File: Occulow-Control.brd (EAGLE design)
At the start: 38.1 x 104.1 mm, 44 parts, among them T1 DMP3010LK3, T2 DMP3010LK3, T3 DMP3010LK3

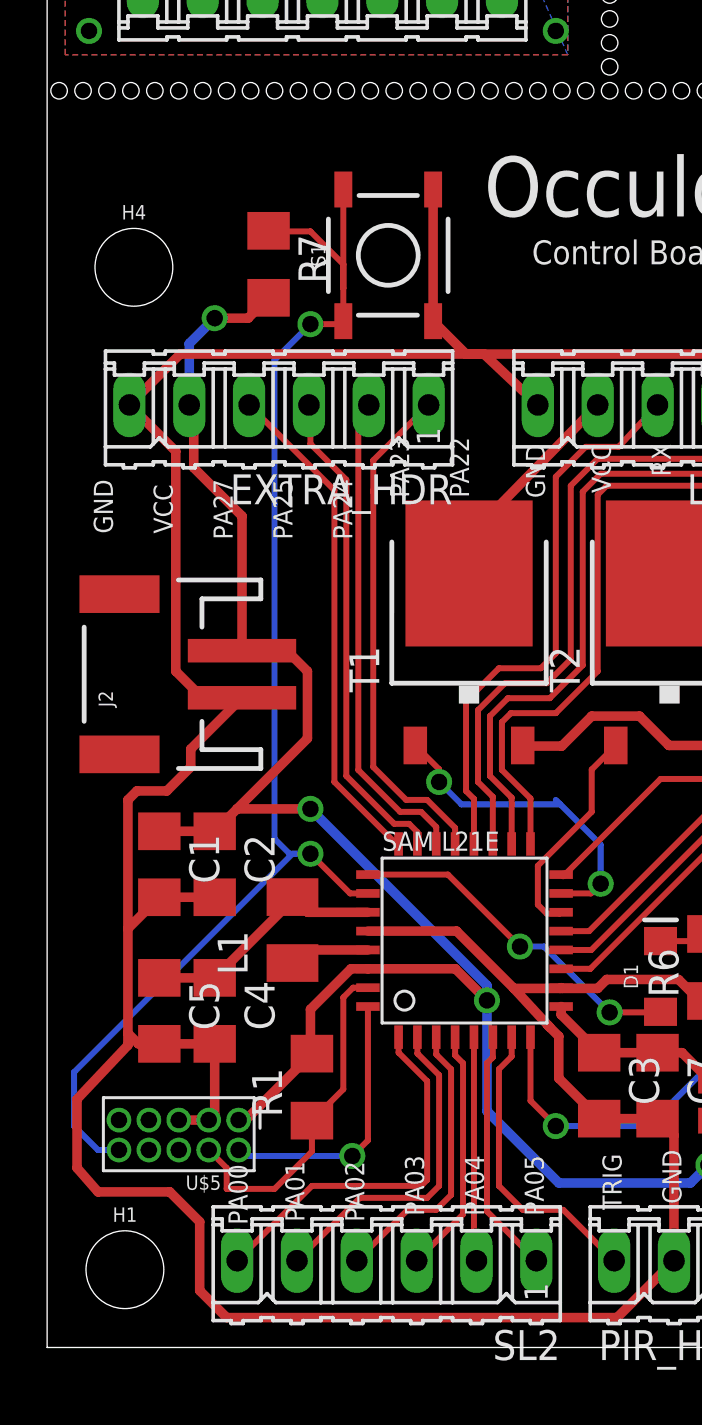
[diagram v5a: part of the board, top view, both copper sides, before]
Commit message: Replaced extra header with JTAG and i2c headers. Fixes #4
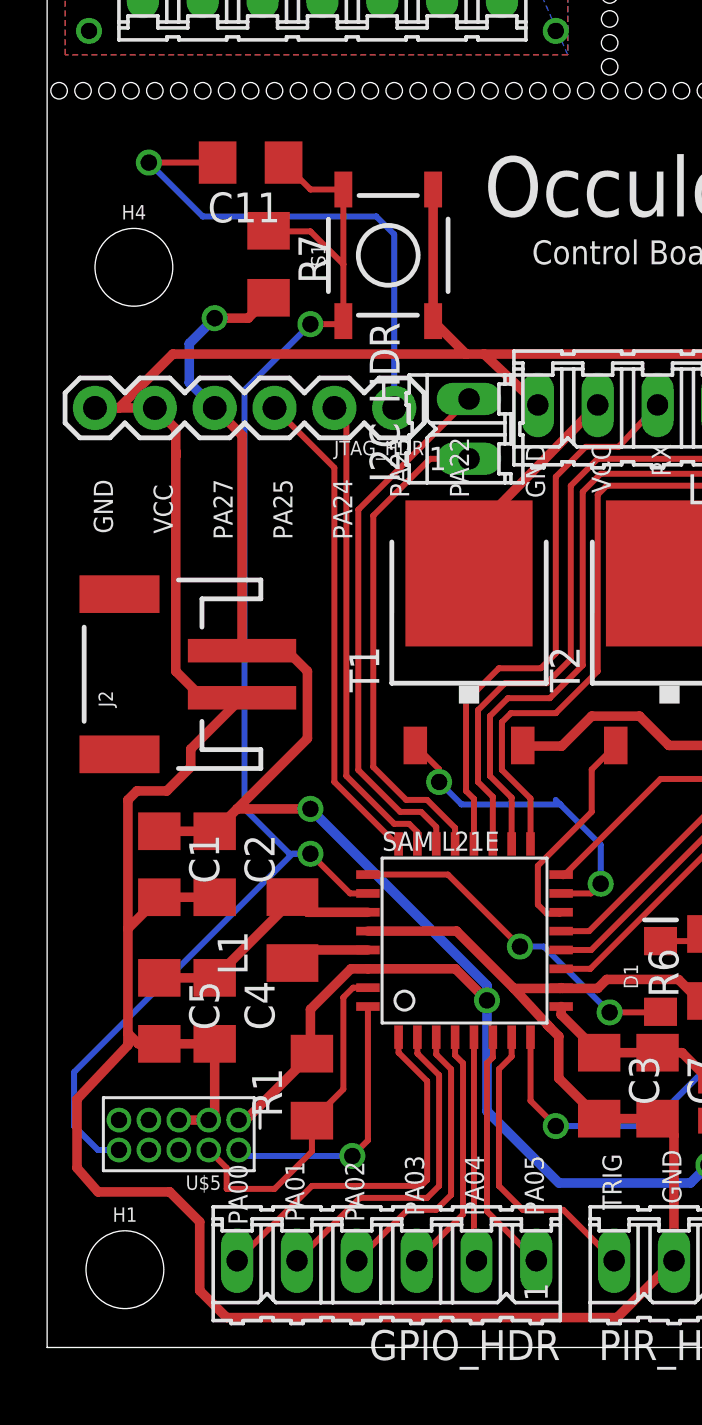
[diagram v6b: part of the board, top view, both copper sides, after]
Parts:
- removed EXTRA_HDR: (no value), con-amp-quick:06P
- added C11: 100nF, rcl:C1206
- added I2C_HDR: (no value), con-amp-quick:02P
- added JTAG_HDR: (no value), SparkFun-Connectors:1X06
- renumbered SL2 to GPIO_HDR
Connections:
- new net DTR: C11.2, JTAG_HDR.1
- net !RESET: now also C11.1
- net GND: now also JTAG_HDR.5, JTAG_HDR.6; no longer EXTRA_HDR.6
- net PA22: now also I2C_HDR.1; no longer EXTRA_HDR.1
- net PA23: now also I2C_HDR.2; no longer EXTRA_HDR.2
- net PA24: now also JTAG_HDR.2; no longer EXTRA_HDR.3
- net PA25: now also JTAG_HDR.3; no longer EXTRA_HDR.4
- net VCC: now also JTAG_HDR.4; no longer EXTRA_HDR.5
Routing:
- net DTR: track 0.00 -> 22.0 mm, vias 0 -> 1
- net !RESET: track 57.7 -> 60.7 mm
- net PA23: track 20.7 -> 22.7 mm
- net GND: track 168.6 -> 170.5 mm
- net PA25: track 21.6 -> 20.7 mm
- net PA22: track 21.6 -> 21.0 mm
- net PA24: track 20.9 -> 20.3 mm

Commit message: Created 2 wire trap lib, placed in schematic
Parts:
- removed J2: (no value), SparkFun-Connectors:JST-2-SMD
- added U$7: MINI-LITE-TRAP, lite-trap:MINI-LITE-TRAP
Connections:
- net GND: now also U$7.3, U$7.4; no longer J2.1
- net VCC: now also U$7.1, U$7.2; no longer J2.2
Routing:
- net GND: track 170.5 -> 149.6 mm
- net VCC: track 107.9 -> 88.5 mm
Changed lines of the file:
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@@
 <?xml version="1.0" encoding="utf-8"?>
 <!DOCTYPE eagle SYSTEM "eagle.dtd">
-<eagle version="8.0.2">
+<eagle version="8.1.0">
 <drawing>
 <settings>
@@
 <setting verticaltext="up"/>
 </settings>
-<grid distance="0.01" unitdist="inch" unit="inch" style="lines" multiple="1" display="no" altdistance="0.005" altunitdist="inch" altunit="inch"/>
+<grid distance="1" unitdist="mm" unit="mm" style="lines" multiple="1" display="no" altdistance="0.05" altunitdist="mm" altunit="mm"/>
 <layers>
 <layer number="1" name="Top" color="4" fill="1" visible="yes" active="yes"/>
@@
 <attribute name="OC_NEWARK" value="unknown" x="34.7345" y="26.4795" size="1.778" layer="27" rot="R90" display="off"/>
 </element>
-<element name="J2" library="SparkFun-Connectors" package="JST-2-SMD" value="" x="4.572" y="28.575" rot="R90">
-<attribute name="PROD_ID" value="CONN-11443" x="4.572" y="28.575" size="1.778" layer="27" rot="R90" display="off"/>
-<attribute name="SF_ID" value="PRT-08612" x="4.572" y="28.575" size="1.778" layer="27" rot="R90" display="off"/>
-</element>
 <element name="L1" library="resistor" package="L3225M" value="10uH" x="10.414" y="17.7165" rot="R90"/>
 <element name="L2" library="SparkFun-Coils" package="0603" value="" x="28.1305" y="10.4775" rot="R270">
@@
 <attribute name="OC_NEWARK" value="unknown" x="17.907" y="38.989" size="1.778" layer="27" rot="R90" display="off"/>
 </element>
+<element name="U$7" library="lite-trap" package="MINI-LITE-TRAP" value="MINI-LITE-TRAP" x="6.5" y="28.25"/>
 </elements>
 <signals>
@@
 <contactref element="GRIDEYE_HDR" pad="5"/>
 <contactref element="PIR_HDR" pad="2"/>
-<contactref element="J2" pad="1"/>
 <contactref element="C7" pad="2"/>
 <contactref element="C1" pad="2"/>
@@
 <wire x1="3.429" y1="17.777" x2="4.7625" y2="19.1105" width="0.4064" layer="1"/>
 <wire x1="3.429" y1="17.777" x2="3.429" y2="23.241" width="0.4064" layer="1"/>
-<wire x1="3.429" y1="23.241" x2="3.81" y2="23.622" width="0.4064" layer="1"/>
-<wire x1="3.81" y1="23.622" x2="5.08" y2="23.622" width="0.4064" layer="1"/>
-<wire x1="5.08" y1="23.622" x2="6.096" y2="24.638" width="0.4064" layer="1"/>
-<wire x1="6.096" y1="24.638" x2="6.096" y2="25.399" width="0.4064" layer="1"/>
-<wire x1="6.096" y1="25.399" x2="8.272" y2="27.575" width="0.4064" layer="1"/>
-<wire x1="8.272" y1="27.575" x2="6.588" y2="27.575" width="0.4064" layer="1"/>
-<wire x1="6.588" y1="27.575" x2="5.461" y2="28.702" width="0.4064" layer="1"/>
 <wire x1="20.828" y1="40.005" x2="18.542" y2="42.164" width="0.4064" layer="1"/>
 <wire x1="3.429" y1="13.335" x2="3.429" y2="12.827" width="0.4064" layer="1"/>
@@
 <wire x1="23.368" y1="15.24" x2="21.8485" y2="15.24" width="0.4064" layer="1"/>
 <wire x1="21.8485" y1="15.24" x2="21.8165" y2="15.272" width="0.4064" layer="1"/>
-<wire x1="5.461" y1="28.702" x2="5.461" y2="37.846" width="0.4064" layer="1"/>
-<wire x1="5.461" y1="37.846" x2="5.461" y2="38.0365" width="0.4064" layer="1"/>
 <contactref element="S1" pad="3"/>
 <contactref element="S1" pad="4"/>
@@
 <contactref element="JTAG_HDR" pad="6"/>
 <contactref element="JTAG_HDR" pad="5"/>
-<wire x1="5.461" y1="37.846" x2="5.461" y2="38.989" width="0.4064" layer="1"/>
 <wire x1="5.461" y1="38.989" x2="4.572" y2="39.878" width="0.4064" layer="1"/>
 <wire x1="3.048" y1="39.878" x2="4.572" y2="39.878" width="0.4064" layer="1"/>
@@
 <wire x1="5.334" y1="42.164" x2="3.048" y2="39.878" width="0.4064" layer="1"/>
 <wire x1="17.78" y1="42.164" x2="5.334" y2="42.164" width="0.4064" layer="1"/>
+<contactref element="U$7" pad="4"/>
+<contactref element="U$7" pad="3"/>
+<wire x1="3.5" y1="25.75" x2="5.461" y2="38.989" width="0" layer="19" extent="1-1"/>
+<wire x1="3.429" y1="23.241" x2="3.5" y2="25.75" width="0" layer="19" extent="1-1"/>
+<wire x1="9.5" y1="25.75" x2="3.429" y2="23.241" width="0" layer="19" extent="1-1"/>
 </signal>
 <signal name="VCC">
-<contactref element="J2" pad="2"/>
 <contactref element="L2" pad="2"/>
 <contactref element="C1" pad="1"/>
@@
 <wire x1="29.464" y1="10.795" x2="29.464" y2="16.605" width="0.4064" layer="1"/>
 <wire x1="30.994" y1="18.135" x2="29.464" y2="16.605" width="0.4064" layer="1"/>
-<wire x1="10.176" y1="29.575" x2="8.272" y2="29.575" width="0.4064" layer="1"/>
-<wire x1="10.176" y1="29.575" x2="11.049" y2="28.702" width="0.4064" layer="1"/>
-<wire x1="11.049" y1="28.702" x2="11.049" y2="25.8475" width="0.4064" layer="1"/>
-<wire x1="8.0615" y1="22.86" x2="11.049" y2="25.8475" width="0.4064" layer="1"/>
 <wire x1="8.0615" y1="22.86" x2="7.112" y2="21.9105" width="0.4064" layer="1"/>
 <wire x1="13.6165" y1="16.072" x2="12.897" y2="16.072" width="0.4064" layer="1"/>
@@
 <contactref element="JTAG_HDR" pad="4"/>
 <wire x1="8.272" y1="38.718" x2="7.112" y2="39.878" width="0.4064" layer="1"/>
-<wire x1="8.272" y1="29.575" x2="8.272" y2="38.718" width="0.4064" layer="1"/>
 <wire x1="6.0325" y1="42.6085" x2="6.0325" y2="40.9575" width="0.4064" layer="16"/>
 <wire x1="6.0325" y1="40.9575" x2="7.112" y2="39.878" width="0.4064" layer="16"/>
+<contactref element="U$7" pad="1"/>
+<contactref element="U$7" pad="2"/>
+<wire x1="9.5" y1="29.75" x2="8.272" y2="38.718" width="0" layer="19" extent="1-1"/>
+<wire x1="3.5" y1="29.75" x2="9.5" y2="29.75" width="0" layer="19" extent="1-1"/>
+<wire x1="8.0615" y1="22.86" x2="9.5" y2="29.75" width="0" layer="19" extent="1-1"/>
 </signal>
 <signal name="RF">

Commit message: Added lib for ldo voltage regulator, placed in schematic. No layout
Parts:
- added C13: 1uF, rcl:C1206
- added U$6: LDO-3V-SOT23-5, Occulow:SOT23-5L
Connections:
- new net N$5: C13.1, U$6.1, U$7.1, U$7.2
- net GND: now also C13.2, U$6.2
- net VCC: now also U$6.5; no longer U$7.1, U$7.2
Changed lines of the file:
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@@
 </element>
 <element name="U$7" library="lite-trap" package="MINI-LITE-TRAP" value="MINI-LITE-TRAP" x="6.5" y="28.25"/>
+<element name="U$6" library="Occulow" package="SOT23-5L" value="LDO-3V-SOT23-5" x="9.4" y="32.8"/>
+<element name="C13" library="rcl" package="C1206" value="1uF" x="2" y="33" rot="R270"/>
 </elements>
 <signals>
@@
 <wire x1="5.334" y1="42.164" x2="3.048" y2="39.878" width="0.4064" layer="1"/>
 <wire x1="17.78" y1="42.164" x2="5.334" y2="42.164" width="0.4064" layer="1"/>
+<contactref element="C13" pad="2"/>
 <contactref element="U$7" pad="4"/>
 <contactref element="U$7" pad="3"/>
+<contactref element="U$6" pad="2"/>
 <wire x1="3.5" y1="25.75" x2="5.461" y2="38.989" width="0" layer="19" extent="1-1"/>
 <wire x1="3.429" y1="23.241" x2="3.5" y2="25.75" width="0" layer="19" extent="1-1"/>
-<wire x1="9.5" y1="25.75" x2="3.429" y2="23.241" width="0" layer="19" extent="1-1"/>
+<wire x1="9.5" y1="25.75" x2="3.5" y2="25.75" width="0" layer="19" extent="1-1"/>
+<wire x1="8.25" y1="32.8" x2="6.477" y2="2.413" width="0" layer="19" extent="1-1"/>
+<wire x1="2" y1="31.6" x2="8.25" y2="32.8" width="0" layer="19" extent="1-1"/>
 </signal>
 <signal name="VCC">
@@
 <wire x1="6.0325" y1="42.6085" x2="6.0325" y2="40.9575" width="0.4064" layer="16"/>
 <wire x1="6.0325" y1="40.9575" x2="7.112" y2="39.878" width="0.4064" layer="16"/>
-<contactref element="U$7" pad="1"/>
-<contactref element="U$7" pad="2"/>
-<wire x1="9.5" y1="29.75" x2="8.272" y2="38.718" width="0" layer="19" extent="1-1"/>
-<wire x1="3.5" y1="29.75" x2="9.5" y2="29.75" width="0" layer="19" extent="1-1"/>
-<wire x1="8.0615" y1="22.86" x2="9.5" y2="29.75" width="0" layer="19" extent="1-1"/>
+<contactref element="U$6" pad="5"/>
+<wire x1="8.0615" y1="22.86" x2="8.272" y2="38.718" width="0" layer="19" extent="1-1"/>
+<wire x1="10.55" y1="33.75" x2="8.128" y2="9.652" width="0" layer="19" extent="1-1"/>
 </signal>
 <signal name="RF">
@@
 <wire x1="4.318" y1="50.292" x2="7.236" y2="50.292" width="0.254" layer="1"/>
 </signal>
+<signal name="N$5">
+<contactref element="U$7" pad="1"/>
+<contactref element="U$7" pad="2"/>
+<contactref element="U$6" pad="1"/>
+<contactref element="C13" pad="1"/>
+<wire x1="3.5" y1="29.75" x2="9.5" y2="29.75" width="0" layer="19" extent="1-1"/>
+<wire x1="8.25" y1="33.75" x2="3.5" y2="29.75" width="0" layer="19" extent="1-1"/>
+<wire x1="2" y1="34.4" x2="8.25" y2="33.75" width="0" layer="19" extent="1-1"/>
+</signal>
 </signals>
